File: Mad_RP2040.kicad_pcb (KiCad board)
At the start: 4 copper layers, 38 x 32.1 mm, 74 parts, among them J1 USB_C_Receptacle, J2 Conn_ARM_SWD_TagConnect_TC203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, Q1 2N7002PV,115, SW1 SW_SPST, SW2 SW_SPST, SW3 EVPAA202K, T1 Tab, T2 Tab, T3 Tab, T4 Tab, U0 PCB, U1 ECMF02-2AMX6, U3 NCP1117-3.3, U4 W25Q128JVSIQ, U5 RP2040, X1 ECS-2520MVLC-120-CN

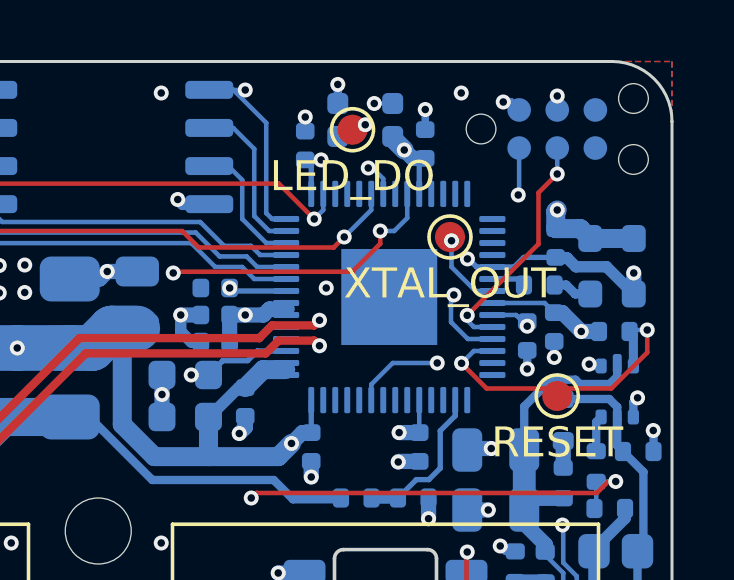
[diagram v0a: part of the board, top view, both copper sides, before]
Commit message: Remove Xtal test pad, update PCB
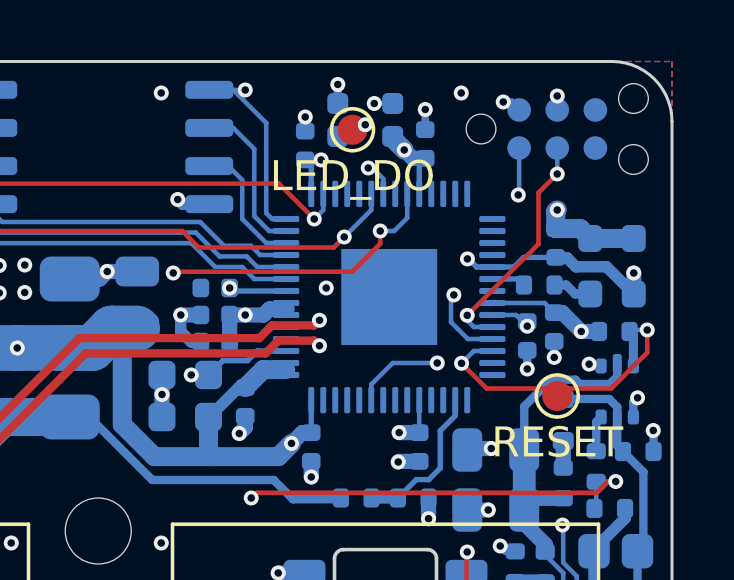
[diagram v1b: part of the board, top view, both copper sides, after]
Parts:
- removed TP5: XTAL_OUT, TestPoint:TestPoint_Pad_D1.0mm
- moved T3 0.12 mm to (159.9, 84.7)
- moved T4 0.10 mm to (140.9, 103.8)
- moved T1 0.10 mm to (140.9, 71.7)
- moved T2 0.05 mm to (121.9, 84.7)
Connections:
- U5 pad 21: Net-(U5-XTAL_OUT) -> unconnected-(U5-XTAL_OUT-Pad21)
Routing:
- net Net-(U5-XTAL_OUT): track 2.57 -> 0.00 mm, vias 1 -> 0

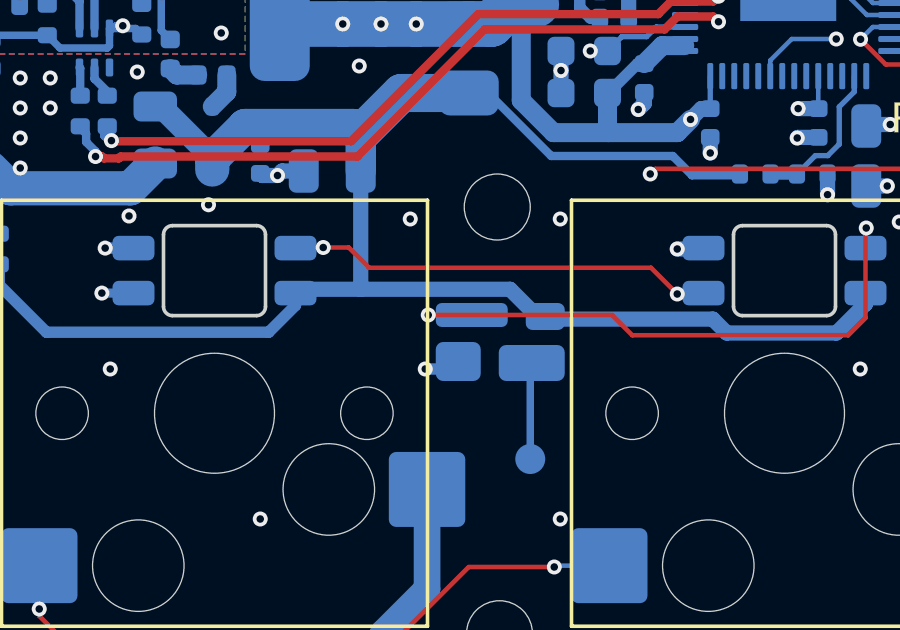
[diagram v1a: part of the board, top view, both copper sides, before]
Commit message: Update footprint on back light SK6812MINI LED, add more back lights.
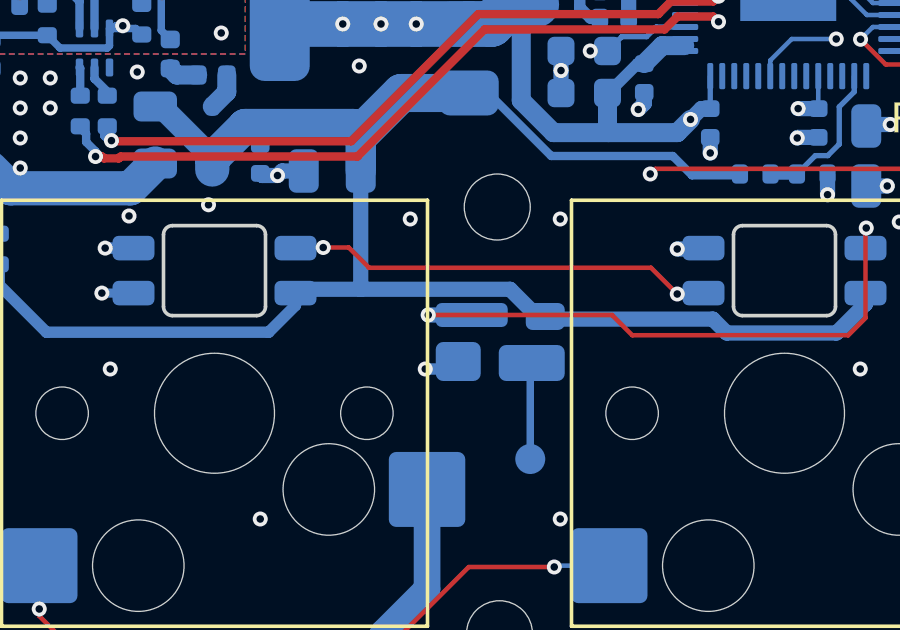
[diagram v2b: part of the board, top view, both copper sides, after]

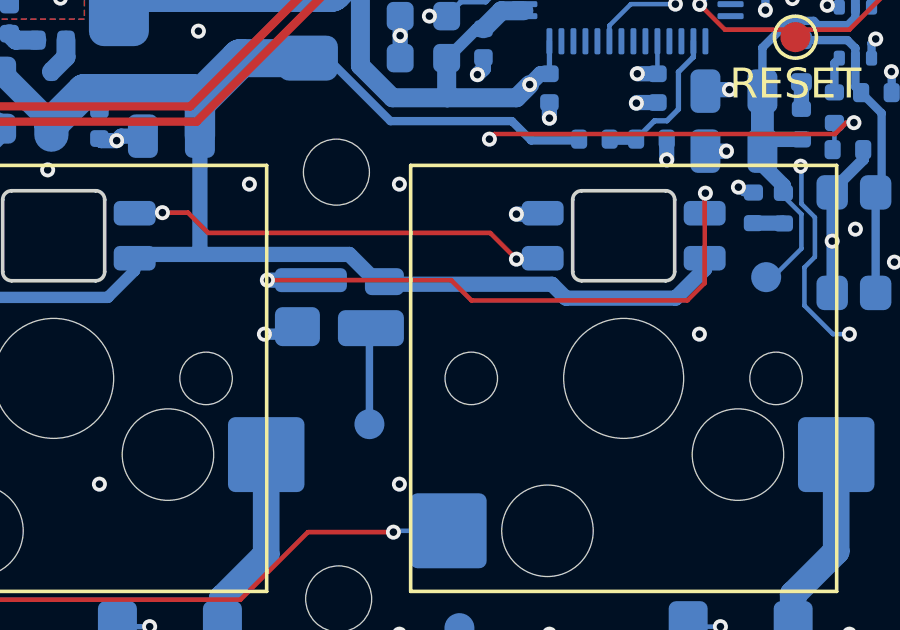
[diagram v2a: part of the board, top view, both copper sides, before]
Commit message: Update PCB back light
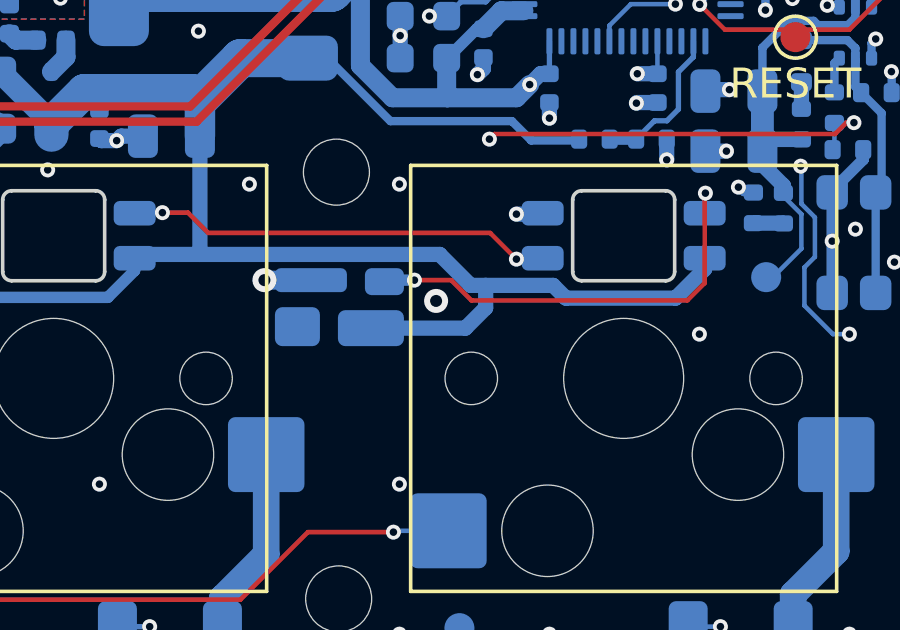
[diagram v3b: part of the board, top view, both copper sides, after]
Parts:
- removed TP3: OUT3, TestPoint:TestPoint_Pad_D1.0mm
- moved T3 0.50 mm to (160.4, 84.7)
- moved T4 0.50 mm to (140.9, 104.3)
- moved T2 0.45 mm to (121.5, 84.7)
- moved T1 0.45 mm to (140.9, 71.3)
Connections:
- D8 pad 1: +5V -> /Out2
- D8 pad 2: /Out3 -> +5V
- D8 pad 3: GND -> unconnected-(D8-DOUT-Pad3)
- D8 pad 4: /Out2 -> GND
- U5 pad 37: /RP2040/STATUS_LED_DO -> /RP2040/RP2040/GPIO25
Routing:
- net /Out2: track 20.2 -> 14.9 mm
- net +5V: track 60.8 -> 65.7 mm
- net /Out3: track 3.22 -> 0.00 mm
- net GND: track 45.9 -> 46.2 mm, vias 70 -> 71

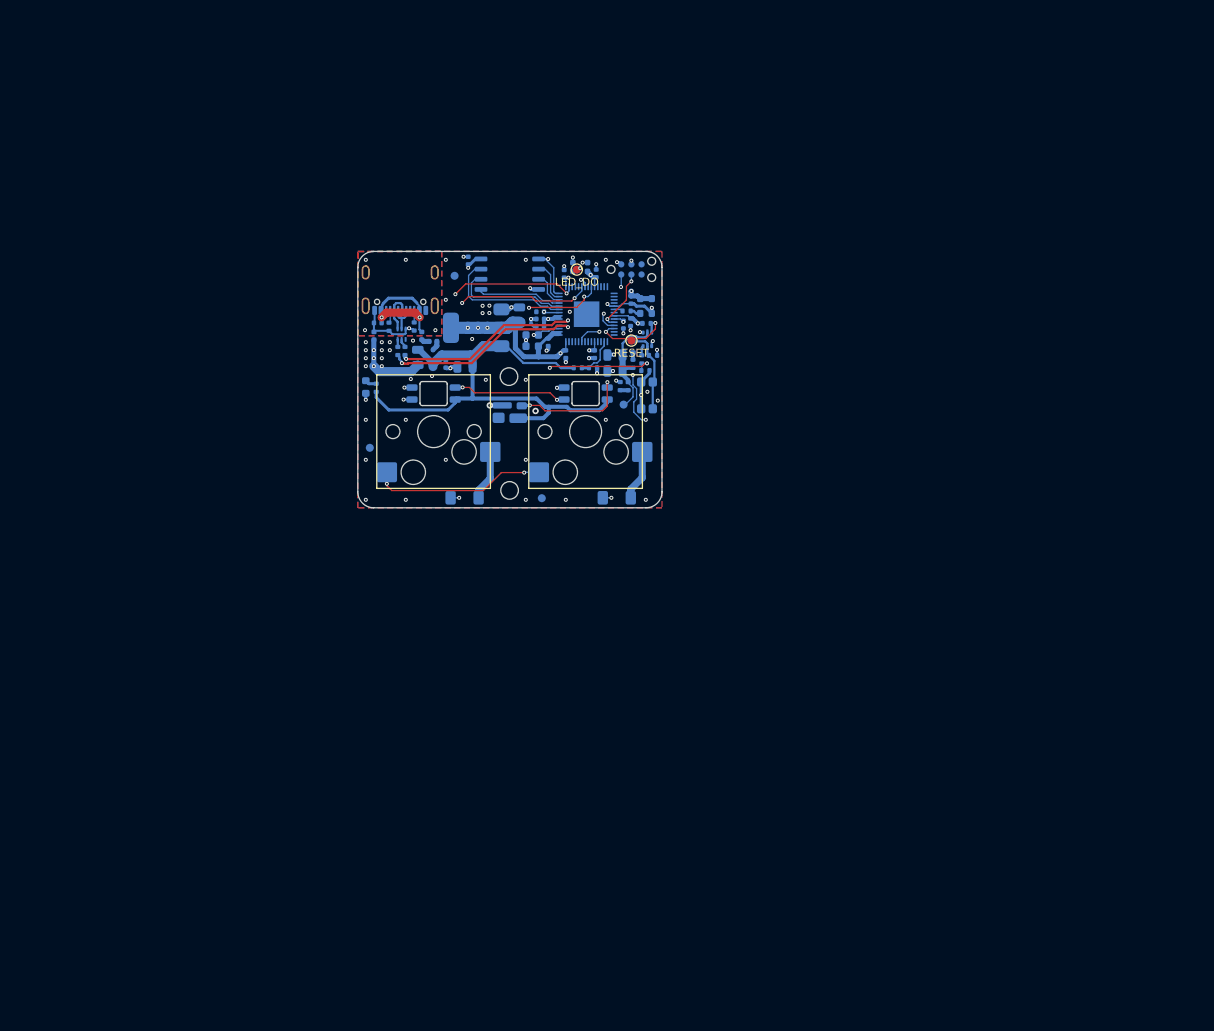
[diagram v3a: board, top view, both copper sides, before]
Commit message: Expand board to 4x5, update rev to b
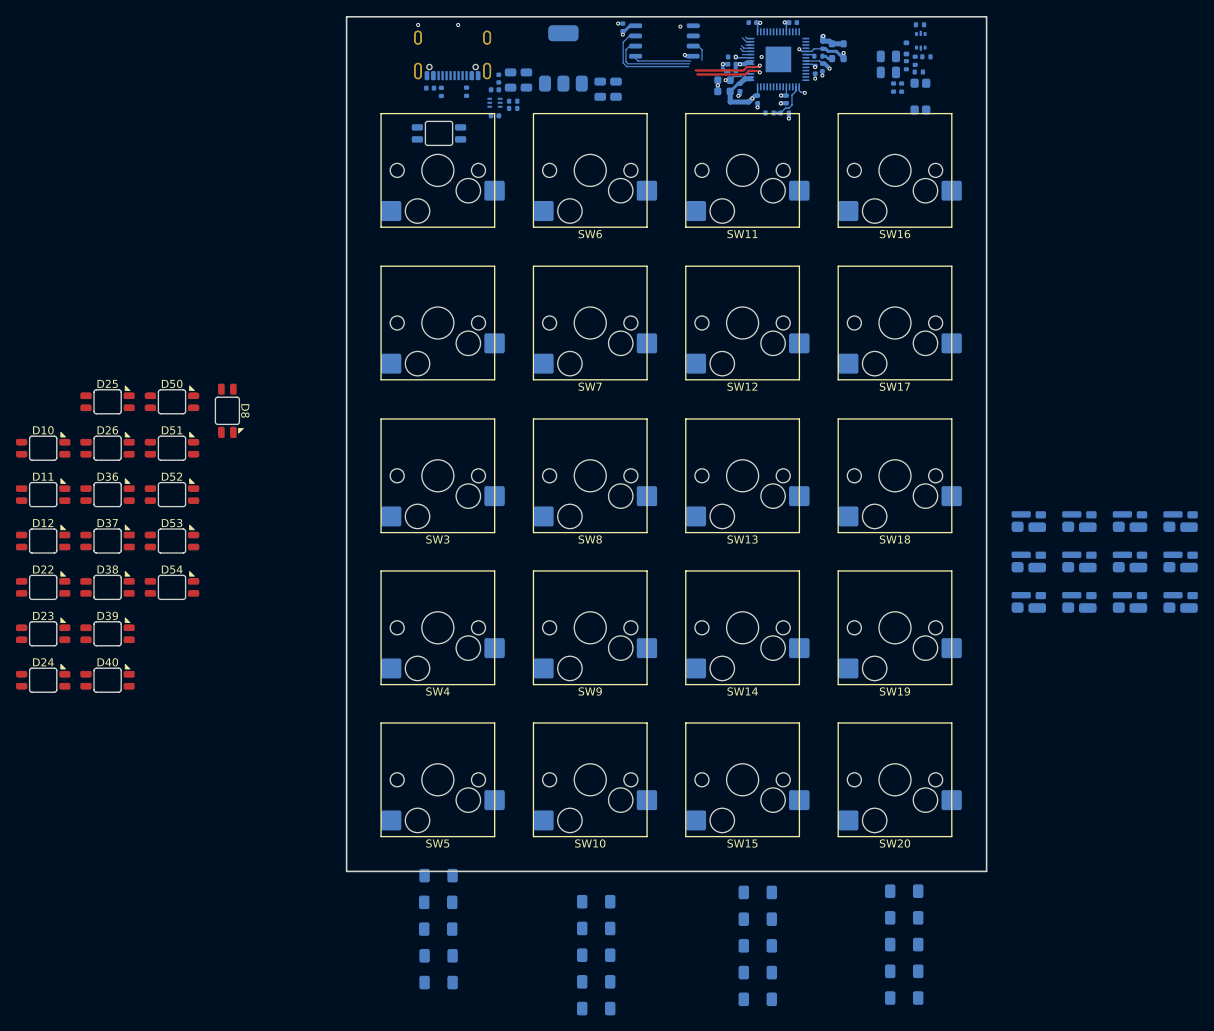
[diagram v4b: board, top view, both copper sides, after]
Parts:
- removed D9: B5817WS, Diode_SMD:D_SOD-323
- removed F1: 500mA, Fuse:Fuse_0402_1005Metric
- removed FID1, FID2, FID3: Fiducial, Fiducial:Fiducial_1mm_Mask2mm
- removed H1, H2: MountingHole_Pad, MountingHole:MountingHole_2.2mm_M2_DIN965
- removed J2: Conn_ARM_SWD_TagConnect_TC2030-NL, Connector:Tag-Connect_TC2030-IDC-NL_2x03_P1.27mm_Vertical
- removed R5: 1K, Resistor_SMD:R_0402_1005Metric
- removed T1, T2, T3, T4: Tab, PCM_kikit:Tab
- removed TP1: RESET, TestPoint:TestPoint_Pad_D1.0mm
- removed TP2: DELAY, TestPoint:TestPoint_Pad_D1.0mm
- removed TP4: LED_DO, TestPoint:TestPoint_Pad_D1.0mm
- removed U0: PCB, Mad_Footprints:BOM
- removed U1: ECMF02-2AMX6, Mad_Footprints:ST_UQFN-6L_1.5x1.7mm_P0.5mm
- added C22: 10uF, Capacitor_SMD:C_0805_2012Metric, B.Cu at (152.2, 51.5)
- added D10: SK6812_MINI_E, Mad_Footprints:SK6812MINI-E, F.Cu at (82.6, 96.3)
- added D11: SK6812_MINI_E, Mad_Footprints:SK6812MINI-E, F.Cu at (82.6, 102.1)
- added D12: SK6812_MINI_E, Mad_Footprints:SK6812MINI-E, F.Cu at (82.6, 107.9)
- added D13: SK6812MINI, Mad_Footprints:SK6812MINI-012, B.Cu at (205.9, 115.4)
- added D14: SK6812MINI, Mad_Footprints:SK6812MINI-012, B.Cu at (205.9, 110.3)
- added D15: SK6812MINI, Mad_Footprints:SK6812MINI-012, B.Cu at (205.9, 105.3)
- added D16: SK6812MINI, Mad_Footprints:SK6812MINI-012, B.Cu at (212.2, 115.4)
- added D17: LL4148, Diode_SMD:D_MiniMELF, B.Cu at (151.8, 166.4)
- added D18: LL4148, Diode_SMD:D_MiniMELF, B.Cu at (151.8, 163.0)
- added D19: LL4148, Diode_SMD:D_MiniMELF, B.Cu at (151.8, 159.7)
- added D20: LL4148, Diode_SMD:D_MiniMELF, B.Cu at (151.8, 156.4)
- added D21: LL4148, Diode_SMD:D_MiniMELF, B.Cu at (151.8, 153.0)
- added D22: SK6812_MINI_E, Mad_Footprints:SK6812MINI-E, F.Cu at (82.6, 113.7)
- added D23: SK6812_MINI_E, Mad_Footprints:SK6812MINI-E, F.Cu at (82.6, 119.5)
- added D24: SK6812_MINI_E, Mad_Footprints:SK6812MINI-E, F.Cu at (82.6, 125.3)
- added D25: SK6812_MINI_E, Mad_Footprints:SK6812MINI-E, F.Cu at (90.7, 90.5)
- added D26: SK6812_MINI_E, Mad_Footprints:SK6812MINI-E, F.Cu at (90.7, 96.3)
- added D27: SK6812MINI, Mad_Footprints:SK6812MINI-012, B.Cu at (212.2, 110.3)
- added D28: SK6812MINI, Mad_Footprints:SK6812MINI-012, B.Cu at (212.2, 105.3)
- added D29: SK6812MINI, Mad_Footprints:SK6812MINI-012, B.Cu at (218.6, 115.4)
- added D30: SK6812MINI, Mad_Footprints:SK6812MINI-012, B.Cu at (218.6, 110.3)
- added D31: LL4148, Diode_SMD:D_MiniMELF, B.Cu at (171.9, 165.2)
- added D32: LL4148, Diode_SMD:D_MiniMELF, B.Cu at (171.9, 161.9)
- added D33: LL4148, Diode_SMD:D_MiniMELF, B.Cu at (171.9, 158.5)
- added D34: LL4148, Diode_SMD:D_MiniMELF, B.Cu at (171.9, 155.2)
- added D35: LL4148, Diode_SMD:D_MiniMELF, B.Cu at (171.9, 151.9)
- added D36: SK6812_MINI_E, Mad_Footprints:SK6812MINI-E, F.Cu at (90.7, 102.1)
- added D37: SK6812_MINI_E, Mad_Footprints:SK6812MINI-E, F.Cu at (90.7, 107.9)
- added D38: SK6812_MINI_E, Mad_Footprints:SK6812MINI-E, F.Cu at (90.7, 113.7)
- added D39: SK6812_MINI_E, Mad_Footprints:SK6812MINI-E, F.Cu at (90.7, 119.5)
- added D40: SK6812_MINI_E, Mad_Footprints:SK6812MINI-E, F.Cu at (90.7, 125.3)
- added D41: SK6812MINI, Mad_Footprints:SK6812MINI-012, B.Cu at (218.6, 105.3)
- added D42: SK6812MINI, Mad_Footprints:SK6812MINI-012, B.Cu at (224.9, 115.4)
- added D43: SK6812MINI, Mad_Footprints:SK6812MINI-012, B.Cu at (224.9, 110.3)
- added D44: SK6812MINI, Mad_Footprints:SK6812MINI-012, B.Cu at (224.9, 105.3)
- added D45: LL4148, Diode_SMD:D_MiniMELF, B.Cu at (190.2, 165.1)
- added D46: LL4148, Diode_SMD:D_MiniMELF, B.Cu at (190.2, 161.7)
- added D47: LL4148, Diode_SMD:D_MiniMELF, B.Cu at (190.2, 158.4)
- added D48: LL4148, Diode_SMD:D_MiniMELF, B.Cu at (190.2, 155.0)
- added D49: LL4148, Diode_SMD:D_MiniMELF, B.Cu at (190.2, 151.7)
- added D50: SK6812_MINI_E, Mad_Footprints:SK6812MINI-E, F.Cu at (98.7, 90.5)
- added D51: SK6812_MINI_E, Mad_Footprints:SK6812MINI-E, F.Cu at (98.7, 96.3)
- added D52: SK6812_MINI_E, Mad_Footprints:SK6812MINI-E, F.Cu at (98.7, 102.1)
- added D53: SK6812_MINI_E, Mad_Footprints:SK6812MINI-E, F.Cu at (98.7, 107.9)
- added D54: SK6812_MINI_E, Mad_Footprints:SK6812MINI-E, F.Cu at (98.7, 113.7)
- added SW10: SW_SPST, Mad_Footprints:SW_Hotswap_Kailh_MX_1.00u, F.Cu at (151.0, 137.8)
- added SW100: EVPAA202K, Mad_Footprints:EVP-AA202K, B.Cu at (192.3, 52.4)
- added SW11: SW_SPST, Mad_Footprints:SW_Hotswap_Kailh_MX_1.00u, F.Cu at (170.1, 61.6)
- added SW12: SW_SPST, Mad_Footprints:SW_Hotswap_Kailh_MX_1.00u, F.Cu at (170.1, 80.7)
- added SW13: SW_SPST, Mad_Footprints:SW_Hotswap_Kailh_MX_1.00u, F.Cu at (170.1, 99.8)
- added SW14: SW_SPST, Mad_Footprints:SW_Hotswap_Kailh_MX_1.00u, F.Cu at (170.1, 118.8)
- added SW15: SW_SPST, Mad_Footprints:SW_Hotswap_Kailh_MX_1.00u, F.Cu at (170.1, 137.8)
- added SW16: SW_SPST, Mad_Footprints:SW_Hotswap_Kailh_MX_1.00u, F.Cu at (189.1, 61.6)
- added SW17: SW_SPST, Mad_Footprints:SW_Hotswap_Kailh_MX_1.00u, F.Cu at (189.1, 80.7)
- added SW18: SW_SPST, Mad_Footprints:SW_Hotswap_Kailh_MX_1.00u, F.Cu at (189.1, 99.8)
- added SW19: SW_SPST, Mad_Footprints:SW_Hotswap_Kailh_MX_1.00u, F.Cu at (189.1, 118.8)
- added SW20: SW_SPST, Mad_Footprints:SW_Hotswap_Kailh_MX_1.00u, F.Cu at (189.1, 137.8)
- added SW4: SW_SPST, Mad_Footprints:SW_Hotswap_Kailh_MX_1.00u, F.Cu at (132.0, 118.8)
- added SW5: SW_SPST, Mad_Footprints:SW_Hotswap_Kailh_MX_1.00u, F.Cu at (132.0, 137.8)
- added SW6: SW_SPST, Mad_Footprints:SW_Hotswap_Kailh_MX_1.00u, F.Cu at (151.0, 61.6)
- added SW7: SW_SPST, Mad_Footprints:SW_Hotswap_Kailh_MX_1.00u, F.Cu at (151.0, 80.7)
- added SW8: SW_SPST, Mad_Footprints:SW_Hotswap_Kailh_MX_1.00u, F.Cu at (151.0, 99.8)
- added SW9: SW_SPST, Mad_Footprints:SW_Hotswap_Kailh_MX_1.00u, F.Cu at (151.0, 118.8)
- added U2: ECMF02-2AMX6, Mad_Footprints:ST_UQFN-6L_1.5x1.7mm_P0.5mm, B.Cu at (139.1, 53.1)
- D3, D4: value SK6812_MINI_E -> LL4148; footprint Mad_Footprints:SK6812MINI-E -> Diode_SMD:D_MiniMELF
- D5: value WS2812C-2020-V1 -> LL4148; footprint Mad_Footprints:WS2812C-2020 -> Diode_SMD:D_MiniMELF
- D6: value GREEN -> SK6812_MINI_E; footprint LED_SMD:LED_0603_1608Metric -> Mad_Footprints:SK6812MINI-E
- D8: value SK6812MINI -> SK6812_MINI_E; footprint Mad_Footprints:SK6812MINI-012 -> Mad_Footprints:SK6812MINI-E; moved to F.Cu
- SW3: value EVPAA202K -> SW_SPST; footprint Mad_Footprints:EVP-AA202K -> Mad_Footprints:SW_Hotswap_Kailh_MX_1.00u; moved to F.Cu
- moved D5 78.1 mm to (132.1, 149.8)
- moved D3 66.9 mm to (132.0, 156.4), turned to 0 degrees
- moved D4 66.2 mm to (132.0, 153.1), turned to 0 degrees
- moved D2 61.4 mm to (132.1, 159.8), turned to 180 degrees
- moved D1 60.7 mm to (132.1, 163.1), turned to 180 degrees
- moved R8 50.6 mm to (190.5, 48.5)
- moved R9 50.6 mm to (189.9, 51.2)
- moved C8 50.6 mm to (188.3, 49.4)
- moved C9 50.6 mm to (188.3, 47.4)
- moved D7 50.6 mm to (190.5, 46.4)
- moved R12 50.6 mm to (191.6, 47.9)
- moved R15 50.6 mm to (188.9, 51.2)
- moved R6 50.6 mm to (193.0, 47.4)
- moved R11 50.6 mm to (192.1, 49.3)
- moved Q1 50.6 mm to (192.3, 45.4)
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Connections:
- D3 pad 1: +5V -> /Row2
- D3 pad 2: /Out1 -> Net-(D3-A)
- D4 pad 1: +5V -> /Row3
- D4 pad 2: /Out2 -> Net-(D4-A)
- D5 pad 1: /RP2040/LED_DO -> /Row4
- D5 pad 2: GND -> Net-(D5-A)
- D6 pad 1: GND -> +5V
- D6 pad 2: Net-(D6-A) -> Net-(D6-DOUT)
- D8 pad 1: /Out2 -> +5V
- D8 pad 2: +5V -> Net-(D10-DIN)
- D8 pad 3: unconnected-(D8-DOUT-Pad3) -> GND
- D8 pad 4: GND -> Net-(D6-DOUT)
- FB1 pad 2: Net-(F1-Pad2) -> +5V
- R3 pad 1: +5V -> /RP2040/3V3
- R3 pad 2: /RP2040/VBUS_DETECT -> /RP2040/RP2040/GPIO18
- R4 pad 1: /RP2040/VBUS_DETECT -> /RP2040/RP2040/GPIO18
- SW3 pad 1: /RP2040/3V3 -> Net-(D3-A)
- SW3 pad 2: Net-(D7-A) -> /Col0
- U5 pad 30: /RP2040/VBUS_DETECT -> /RP2040/RP2040/GPIO19
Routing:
- net +5V: track 65.7 -> 0.00 mm
- net /Col0: track 52.7 -> 0.00 mm, vias 4 -> 0
- net /Row0: track 44.0 -> 0.00 mm, vias 3 -> 0
- net /RP2040/RP2040/QSPI_~{CS}: track 35.2 -> 1.54 mm, vias 3 -> 0
- net /TX0: track 32.8 -> 0.00 mm, vias 3 -> 0
- net /Row1: track 32.0 -> 0.00 mm, vias 2 -> 0
- net GND: track 46.2 -> 16.1 mm, vias 71 -> 14
- net /RP2040/3V3: track 57.6 -> 28.5 mm, vias 13 -> 8
- net /RP2040/~{RST}: track 20.3 -> 0.00 mm, vias 3 -> 0
- net VBUS: track 17.3 -> 0.00 mm, vias 2 -> 0
- net /RP2040/RP2040/USB_D-: track 25.3 -> 9.25 mm, vias 2 -> 1
- net /Out2: track 14.9 -> 0.00 mm, vias 2 -> 0
- net /RP2040/RP2040/USB_D+: track 24.1 -> 9.46 mm, vias 2 -> 1
- net /Out1: track 14.3 -> 0.00 mm, vias 2 -> 0
- net Net-(Q1B-G): track 14.1 -> 0.00 mm
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- removed copper zone on B.Cu, net /PreFIlterGND
- removed copper zone on F.Cu, net /PreFIlterGND
- removed copper zone on In1.Cu, net /PreFIlterGND
- removed copper zone on In2.Cu, net /PreFIlterGND
- removed copper zone on In1.Cu, net /RP2040/3V3
- removed copper zone on In1.Cu, net /RP2040/RP2040/1V1
- removed copper zone on B.Cu, net GND
- removed copper zone on F.Cu, net GND
- removed copper zone on In1.Cu, net GND
- removed copper zone on In2.Cu, net GND
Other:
- board size 38 x 32.1 mm -> 80 x 106.8 mm
